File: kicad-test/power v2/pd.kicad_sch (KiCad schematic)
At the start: 17 parts, among them J1 USB_PD, U1 TPS25730AD

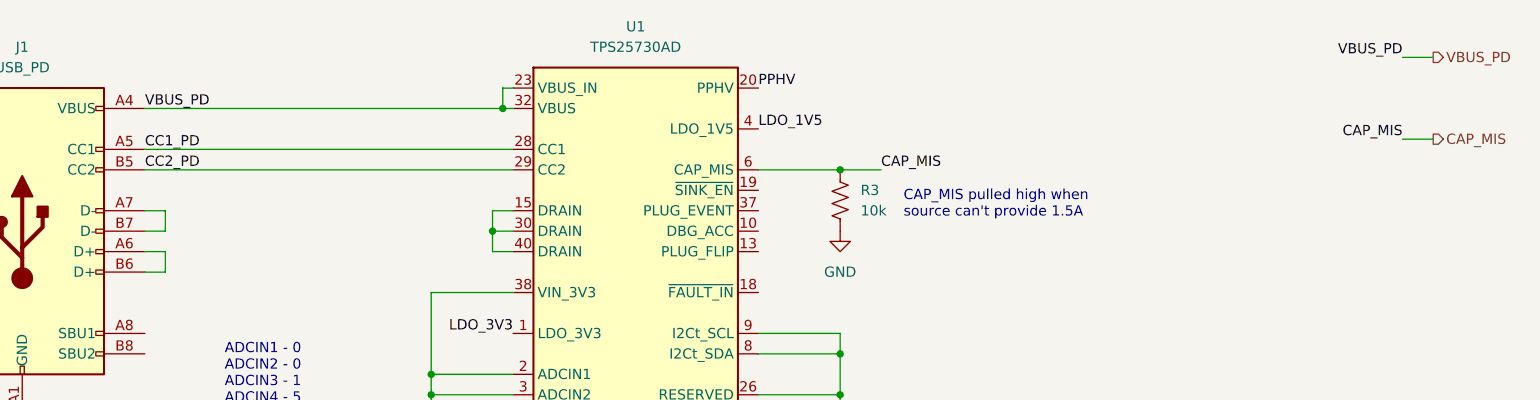
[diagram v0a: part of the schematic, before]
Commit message: usb device connection
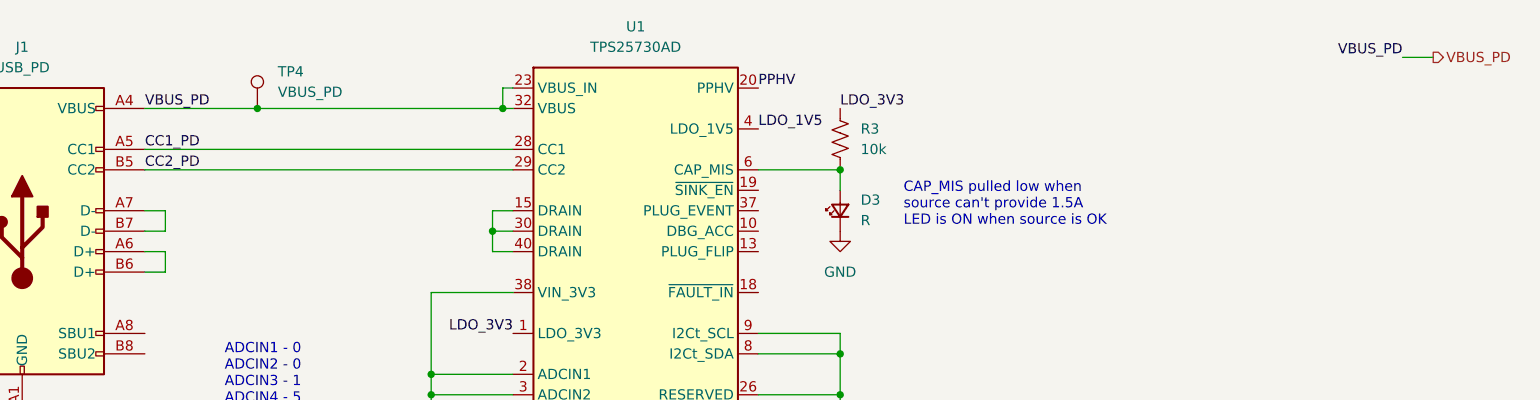
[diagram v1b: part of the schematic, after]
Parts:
- added D3: R, symbol Device:LED_Small
- added TP4: VBUS_PD, symbol Connector:TestPoint
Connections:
- net GND: now also D3.1 (K); no longer R3.1
- net LDO_3V3: now also R3.2
- net VBUS_PD: now also TP4.1
- net CAP_MIS: no longer names the net of U1.6 (CAP_MIS)
- net CAP_MIS: now also R3.1, D3.2 (A); no longer R3.2
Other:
- note added: "CAP_MIS pulled low when source can't provide 1.5A LED is ON when source is OK"
- note removed: "CAP_MIS pulled high when source can't provide 1.5A"
- moved on the sheet: R3

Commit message: add footprints
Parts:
- C1, C10, C11, C12, C2, C3, C4, C5, C6, C7, C8, C9: footprint (none) -> Capacitor_SMD:C_0805_2012Metric_Pad1.18x1.45mm_HandSolder
- D3: footprint (none) -> LED_SMD:LED_0805_2012Metric_Pad1.15x1.40mm_HandSolder
- J1: footprint (none) -> Connector_USB:USB_C_Receptacle_HRO_TYPE-C-31-M-12
- R3, R4, R5: footprint (none) -> Resistor_SMD:R_0805_2012Metric_Pad1.20x1.40mm_HandSolder
- TP4: footprint (none) -> TestPoint:TestPoint_Loop_D3.80mm_Drill2.0mm
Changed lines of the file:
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@@
 			)
 		)
-		(property "Footprint" ""
+		(property "Footprint" "Connector_USB:USB_C_Receptacle_HRO_TYPE-C-31-M-12"
 			(at 60.96 50.8 0)
 			(hide yes)
@@
 			)
 		)
-		(property "Footprint" ""
+		(property "Footprint" "Capacitor_SMD:C_0805_2012Metric_Pad1.18x1.45mm_HandSolder"
 			(at 113.03 100.33 0)
 			(hide yes)
@@
 			)
 		)
-		(property "Footprint" ""
+		(property "Footprint" "Capacitor_SMD:C_0805_2012Metric_Pad1.18x1.45mm_HandSolder"
 			(at 186.69 100.33 0)
 			(hide yes)
@@
 			)
 		)
-		(property "Footprint" ""
+		(property "Footprint" "Capacitor_SMD:C_0805_2012Metric_Pad1.18x1.45mm_HandSolder"
 			(at 172.72 100.33 0)
 			(hide yes)
@@
 			)
 		)
-		(property "Footprint" ""
+		(property "Footprint" "Capacitor_SMD:C_0805_2012Metric_Pad1.18x1.45mm_HandSolder"
 			(at 92.71 100.33 0)
 			(hide yes)
@@
 			)
 		)
-		(property "Footprint" ""
+		(property "Footprint" "Capacitor_SMD:C_0805_2012Metric_Pad1.18x1.45mm_HandSolder"
 			(at 158.75 100.33 0)
 			(hide yes)
@@
 			)
 		)
-		(property "Footprint" ""
+		(property "Footprint" "Capacitor_SMD:C_0805_2012Metric_Pad1.18x1.45mm_HandSolder"
 			(at 127 100.33 0)
 			(hide yes)
@@
 			)
 		)
-		(property "Footprint" ""
+		(property "Footprint" "Resistor_SMD:R_0805_2012Metric_Pad1.20x1.40mm_HandSolder"
 			(at 49.53 100.33 0)
 			(hide yes)
@@
 			)
 		)
-		(property "Footprint" ""
+		(property "Footprint" "Capacitor_SMD:C_0805_2012Metric_Pad1.18x1.45mm_HandSolder"
 			(at 102.87 100.33 0)
 			(hide yes)
@@
 			)
 		)
-		(property "Footprint" ""
+		(property "Footprint" "Capacitor_SMD:C_0805_2012Metric_Pad1.18x1.45mm_HandSolder"
 			(at 82.55 100.33 0)
 			(hide yes)
@@
 			)
 		)
-		(property "Footprint" ""
+		(property "Footprint" "LED_SMD:LED_0805_2012Metric_Pad1.15x1.40mm_HandSolder"
 			(at 158.75 48.26 90)
 			(hide yes)
@@
 			)
 		)
-		(property "Footprint" ""
+		(property "Footprint" "Resistor_SMD:R_0805_2012Metric_Pad1.20x1.40mm_HandSolder"
 			(at 49.53 107.95 0)
 			(hide yes)
@@
 			)
 		)
-		(property "Footprint" ""
+		(property "Footprint" "Capacitor_SMD:C_0805_2012Metric_Pad1.18x1.45mm_HandSolder"
 			(at 207.01 100.33 0)
 			(hide yes)
@@
 			)
 		)
-		(property "Footprint" ""
+		(property "Footprint" "TestPoint:TestPoint_Loop_D3.80mm_Drill2.0mm"
 			(at 91.44 35.56 0)
 			(hide yes)
@@
 			)
 		)
-		(property "Footprint" ""
+		(property "Footprint" "Capacitor_SMD:C_0805_2012Metric_Pad1.18x1.45mm_HandSolder"
 			(at 72.39 100.33 0)
 			(hide yes)
@@
 			)
 		)
-		(property "Footprint" ""
+		(property "Footprint" "Capacitor_SMD:C_0805_2012Metric_Pad1.18x1.45mm_HandSolder"
 			(at 140.97 100.33 0)
 			(hide yes)
@@
 			)
 		)
-		(property "Footprint" ""
+		(property "Footprint" "Resistor_SMD:R_0805_2012Metric_Pad1.20x1.40mm_HandSolder"
 			(at 157.734 39.116 90)
 			(hide yes)
@@
 			)
 		)
-		(property "Footprint" ""
+		(property "Footprint" "Capacitor_SMD:C_0805_2012Metric_Pad1.18x1.45mm_HandSolder"
 			(at 196.85 100.33 0)
 			(hide yes)

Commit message: pcb layout
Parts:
- added J3: D_PIN, Connector_PinHeader_1.00mm:PinHeader_1x02_P1.00mm_Vertical, symbol Connector:Conn_01x02_Pin
- TP1: renamed from TP4; footprint TestPoint:TestPoint_Loop_D3.80mm_Drill2.0mm -> TestPoint:TestPoint_Pad_1.5x1.5mm
- renumbered C5 to C1, C7 to C10, C6 to C2, C8 to C3, C9 to C4, C10 to C5, C1 to C6, C2 to C7, C3 to C8, C4 to C9, D3 to D2, J1 to J2, R4 to R2, R5 to R3, R3 to R4
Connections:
- net at J2.A6 (D+), J2.B6 (D+): now also J3.2 (Pin_2)
- net at J2.A7 (D-), J2.B7 (D-): now also J3.1 (Pin_1)
